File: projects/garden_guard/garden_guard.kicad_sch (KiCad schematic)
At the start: 12 parts, among them J11 USB_C_Receptacle_USB2.0

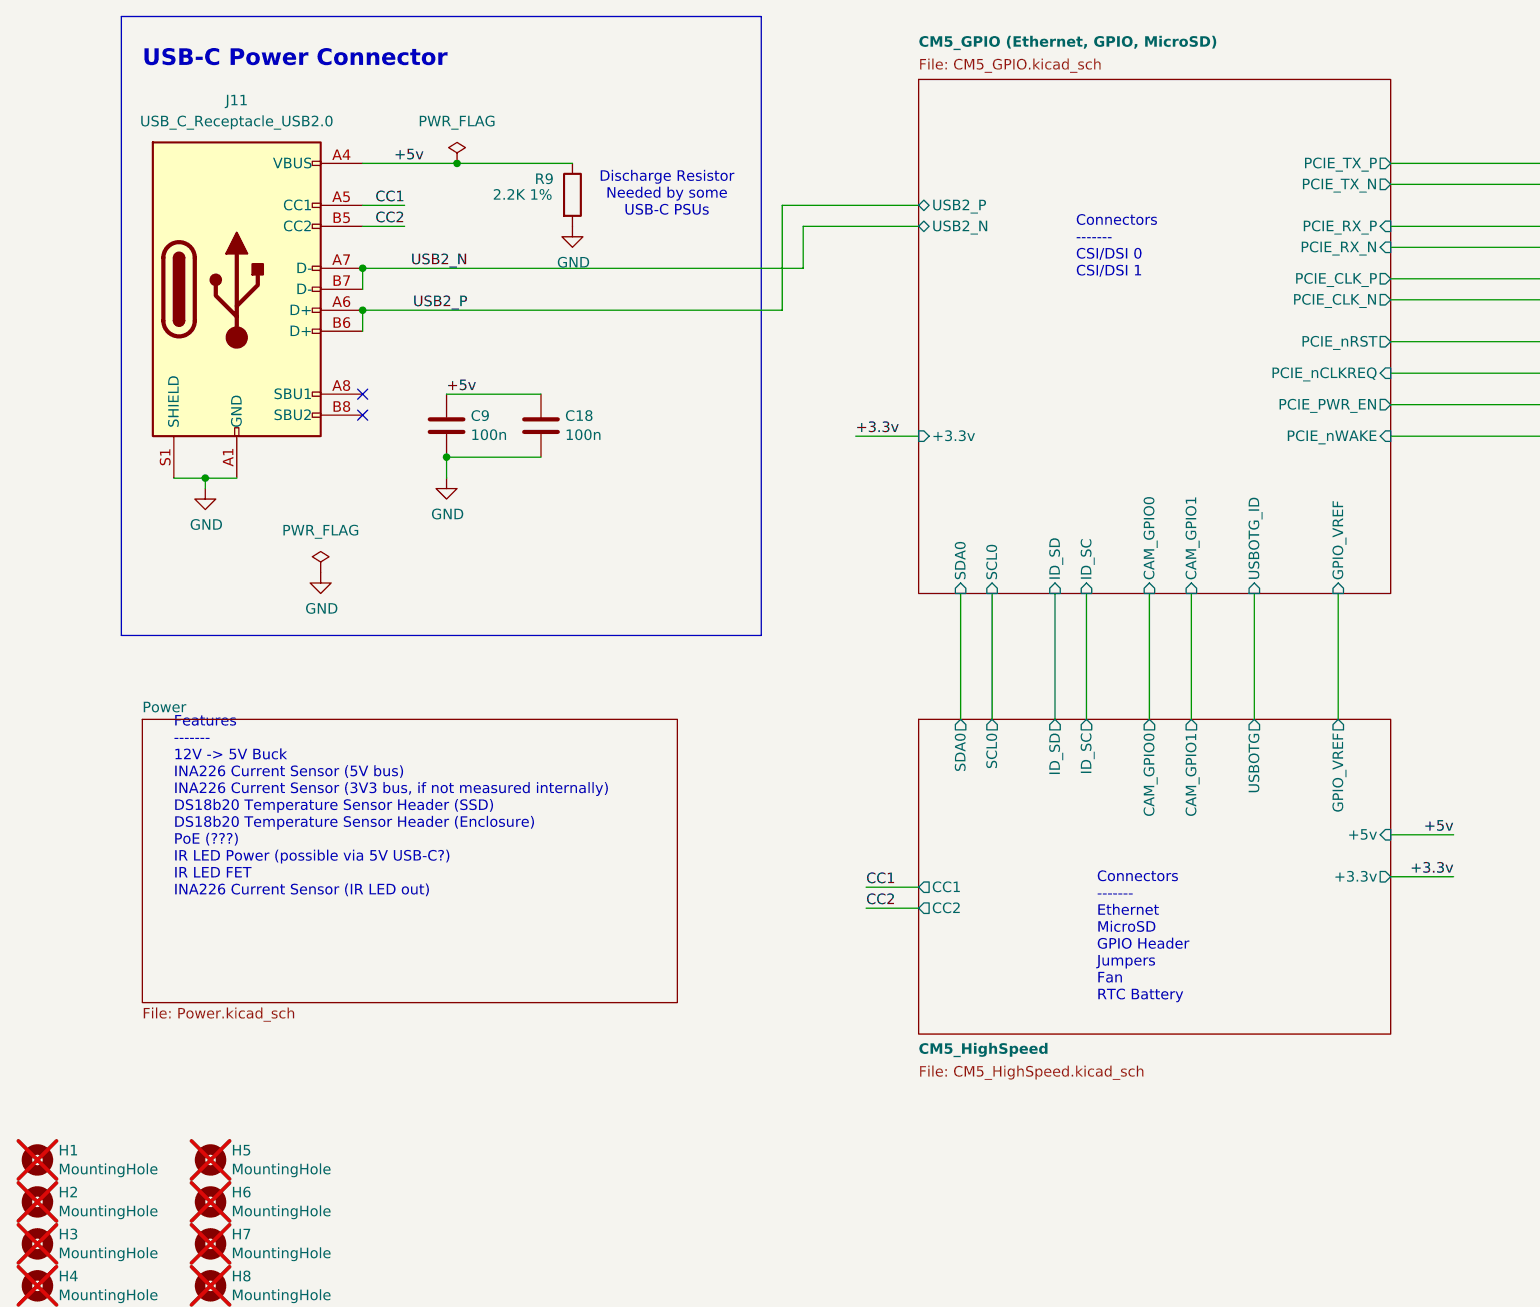
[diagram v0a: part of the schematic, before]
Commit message: - Add PoE 12V power module - Add 12V->5V buck - Add automatic power source selection between PoE 5V and USB 5V
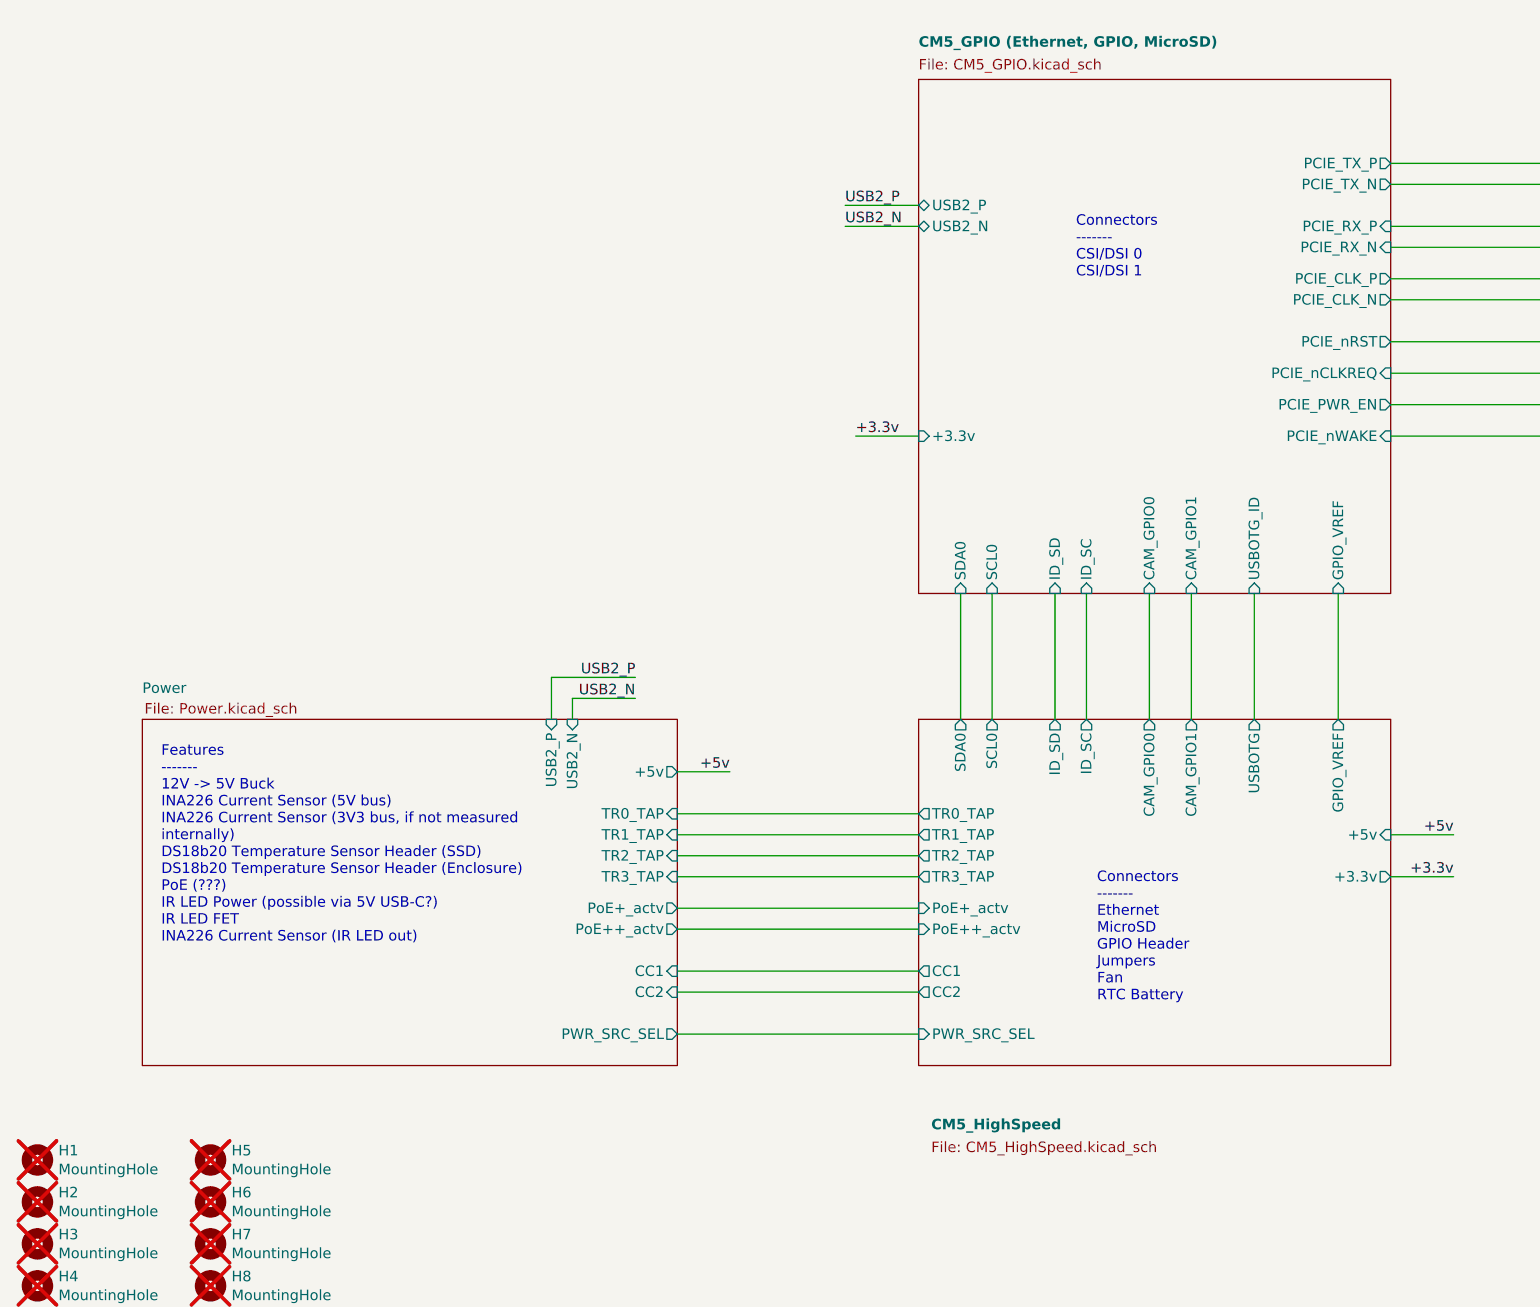
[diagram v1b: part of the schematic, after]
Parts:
- removed C18, C9: 100n, Capacitor_SMD:C_0402_1005Metric, symbol Device:C
- removed J11: USB_C_Receptacle_USB2.0, Connector_USB:USB_C_Receptacle_GCT_USB4105-xx-A_16P_TopMnt_Horizontal, symbol Connector:USB_C_Receptacle_USB2.0_16P
- removed R9: 2.2K 1%, Resistor_SMD:R_0402_1005Metric, symbol Device:R
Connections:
- no-connect marks 2 -> 0
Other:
- sheet CM5_HighSpeed ports: added PWR_SRC_SEL, PoE++_actv, PoE+_actv, TR0_TAP, TR1_TAP, TR2_TAP, TR3_TAP; removed none
- sheet Power ports: added +5v, CC1, CC2, PWR_SRC_SEL, PoE++_actv, PoE+_actv, TR0_TAP, TR1_TAP, TR2_TAP, TR3_TAP, USB2_N, USB2_P; removed none
- note removed: "Discharge Resistor Needed by some USB-C PSUs"
- note removed: "USB-C Power Connector"

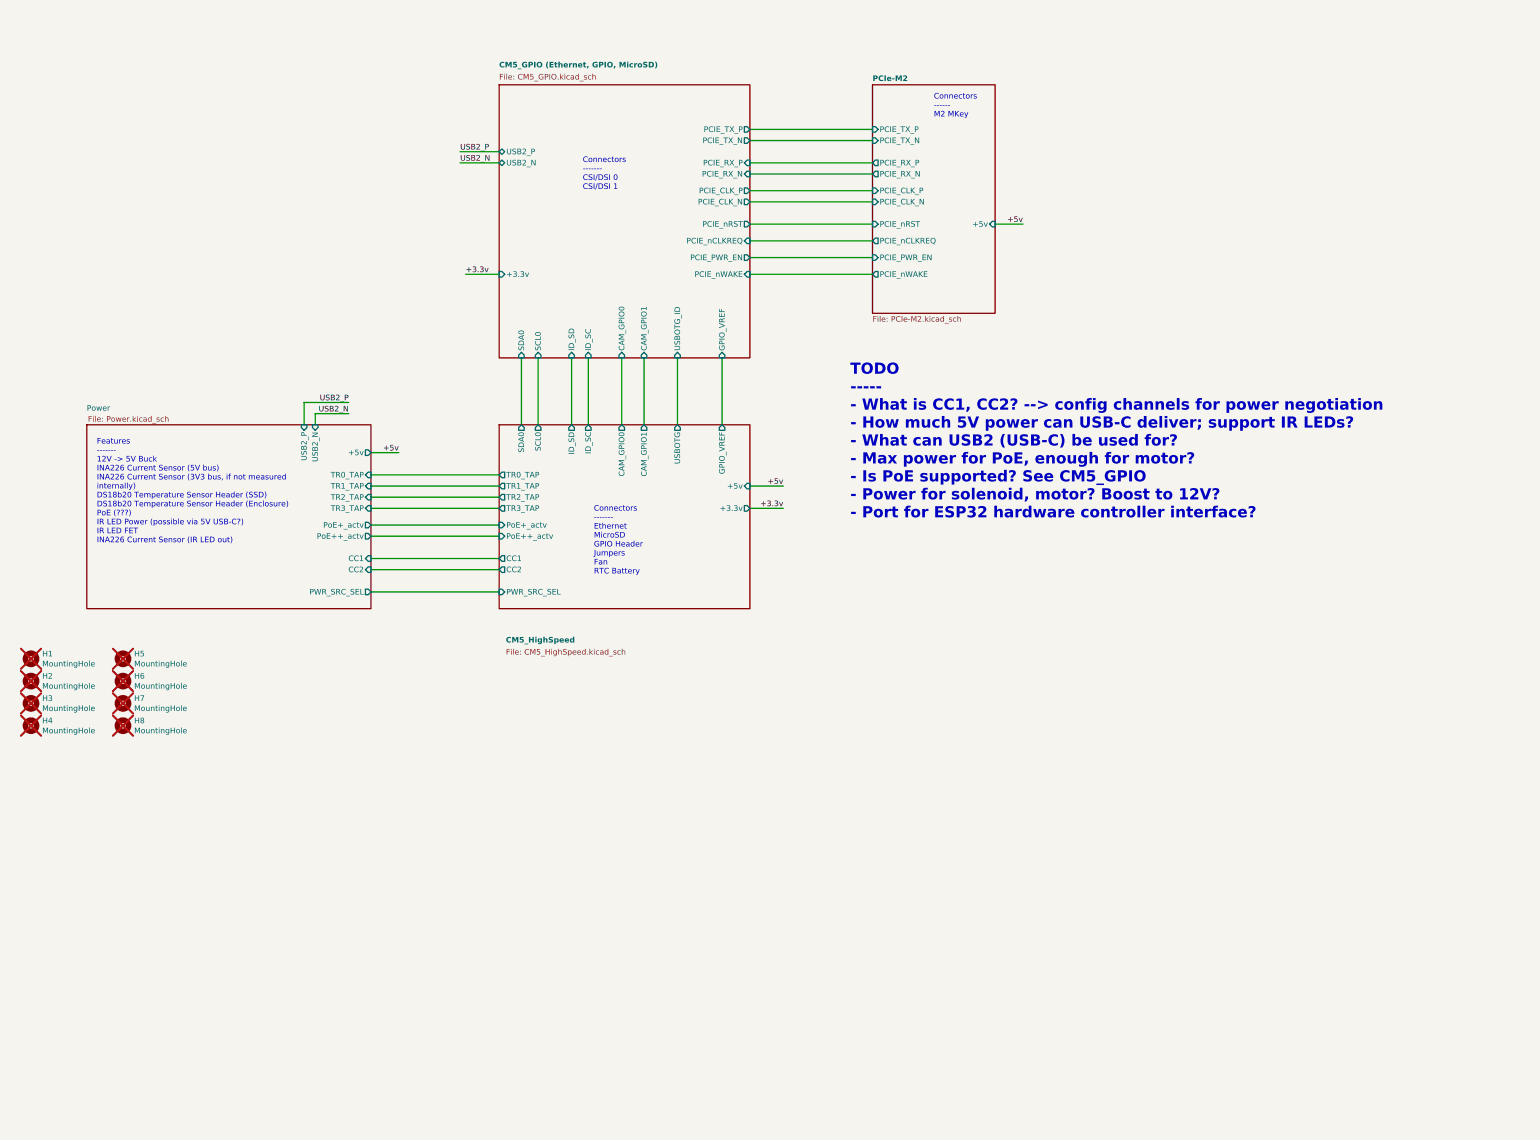
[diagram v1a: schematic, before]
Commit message: - Add 12V and 5V power sensing - Add solenoid and IR illum outputs, power expansion, an peripheral comms - General clean-up - Remove .bak files mistakenly added in previous commits - Add *.bak to .gitignore
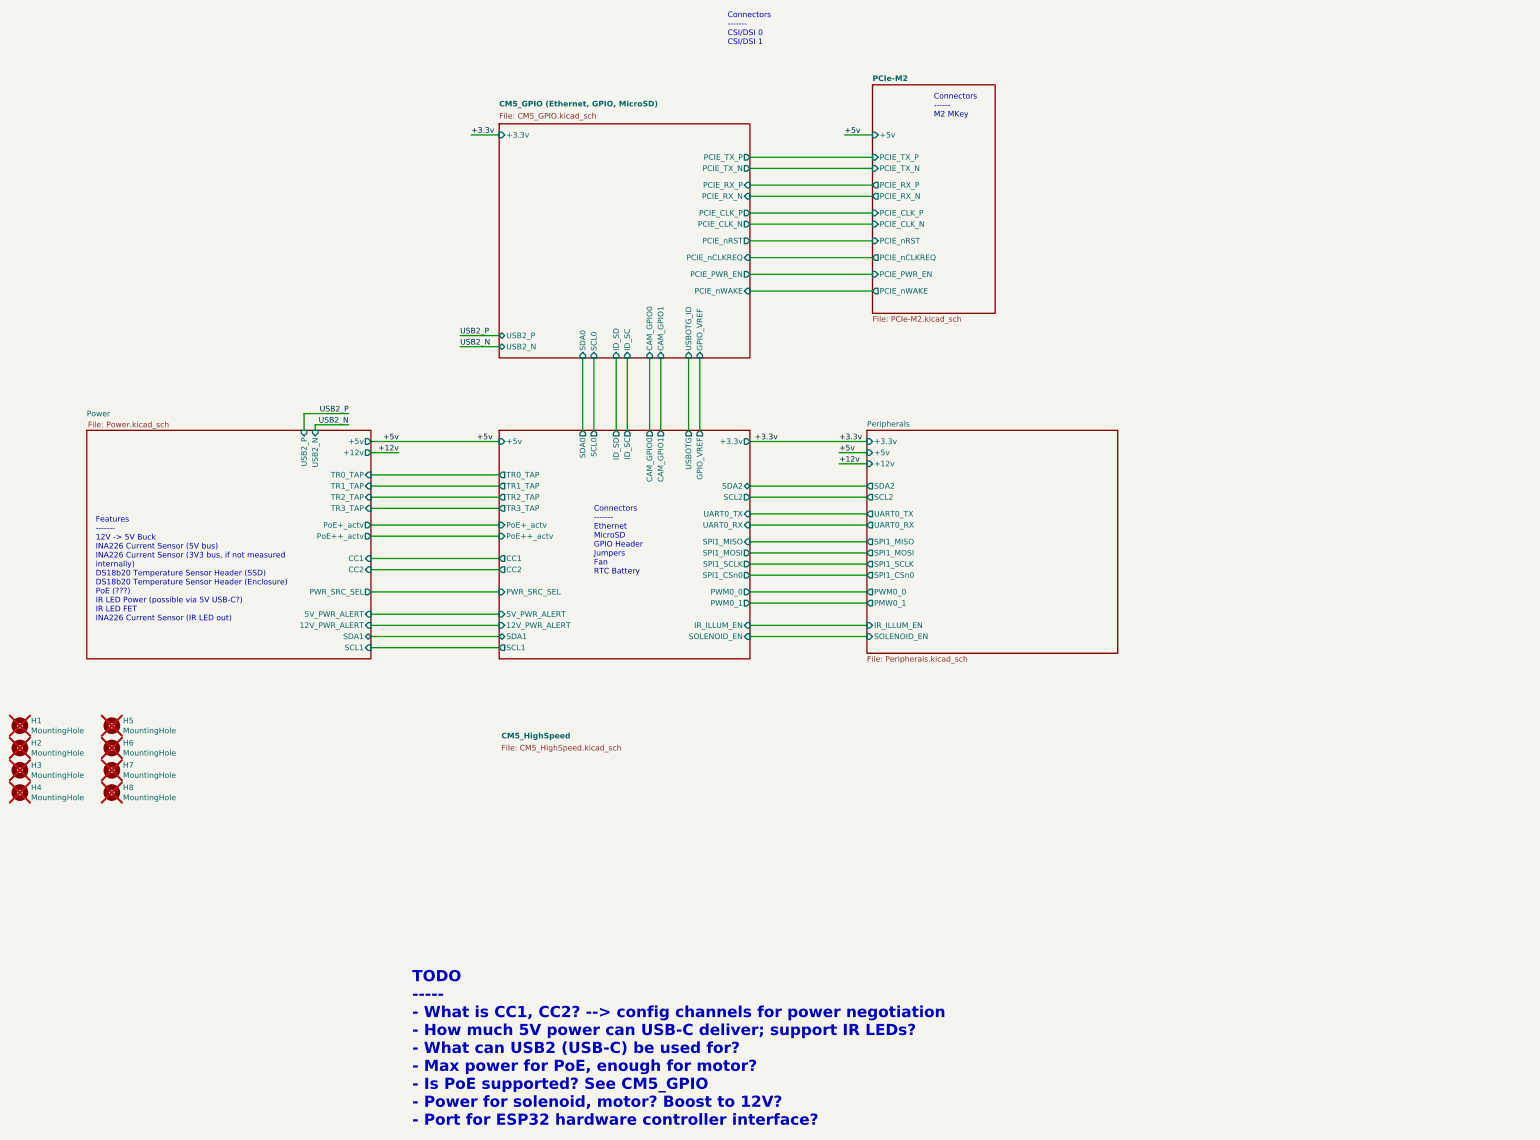
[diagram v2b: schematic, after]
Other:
- added sheet Peripherals (Peripherals.kicad_sch)
- sheet CM5_HighSpeed ports: added 12V_PWR_ALERT, 5V_PWR_ALERT, IR_ILLUM_EN, PWM0_0, PWM0_1, SCL1, SCL2, SDA1, SDA2, SOLENOID_EN, SPI1_CSn0, SPI1_MISO, SPI1_MOSI, SPI1_SCLK, UART0_RX, UART0_TX; removed none
- sheet Power ports: added +12v, 12V_PWR_ALERT, 5V_PWR_ALERT, SCL1, SDA1; removed none
- moved on the sheet: H1, H2, H3, H4, H5, H6, H7, H8

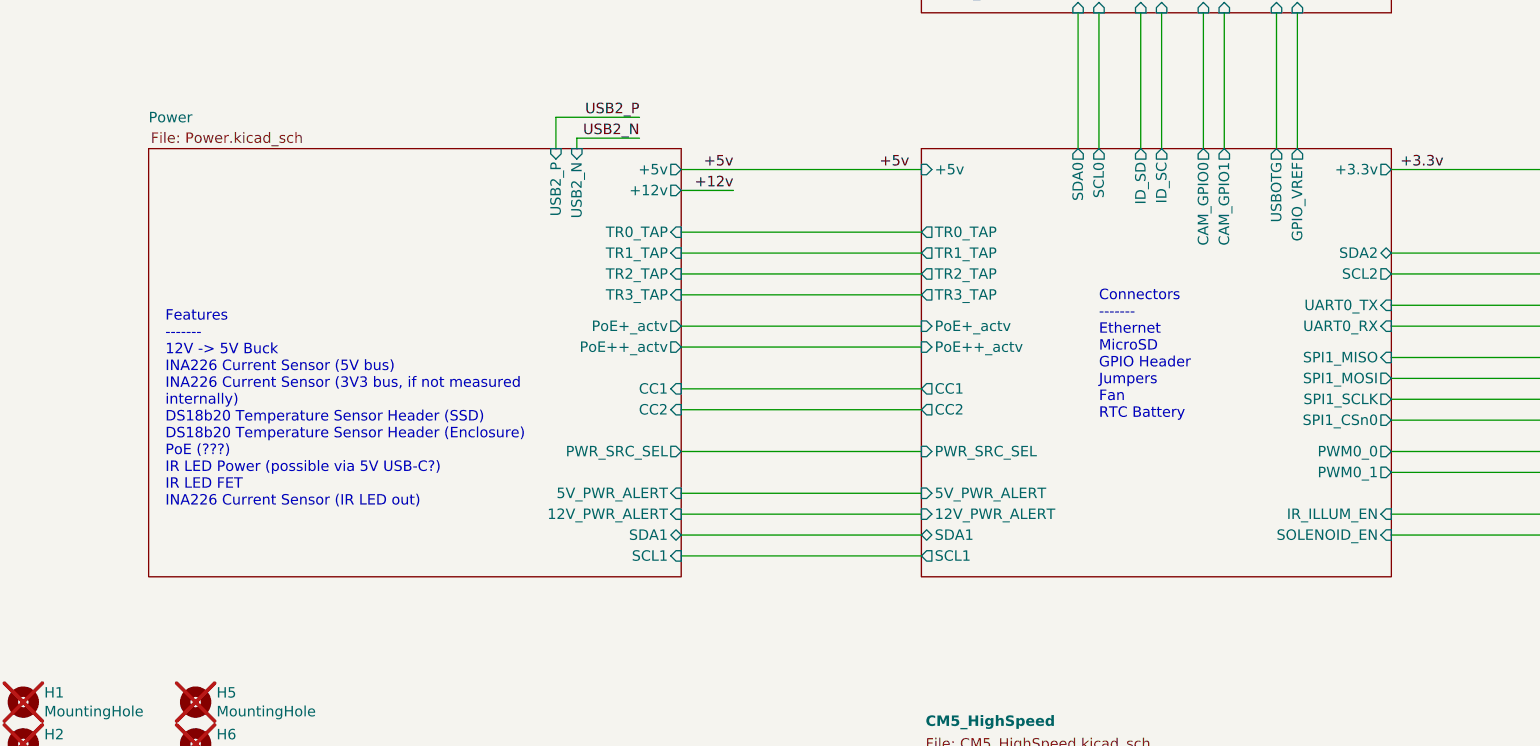
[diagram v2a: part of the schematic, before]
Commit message: - Add all missing footprints - Add specific part numbers to each component in schematic
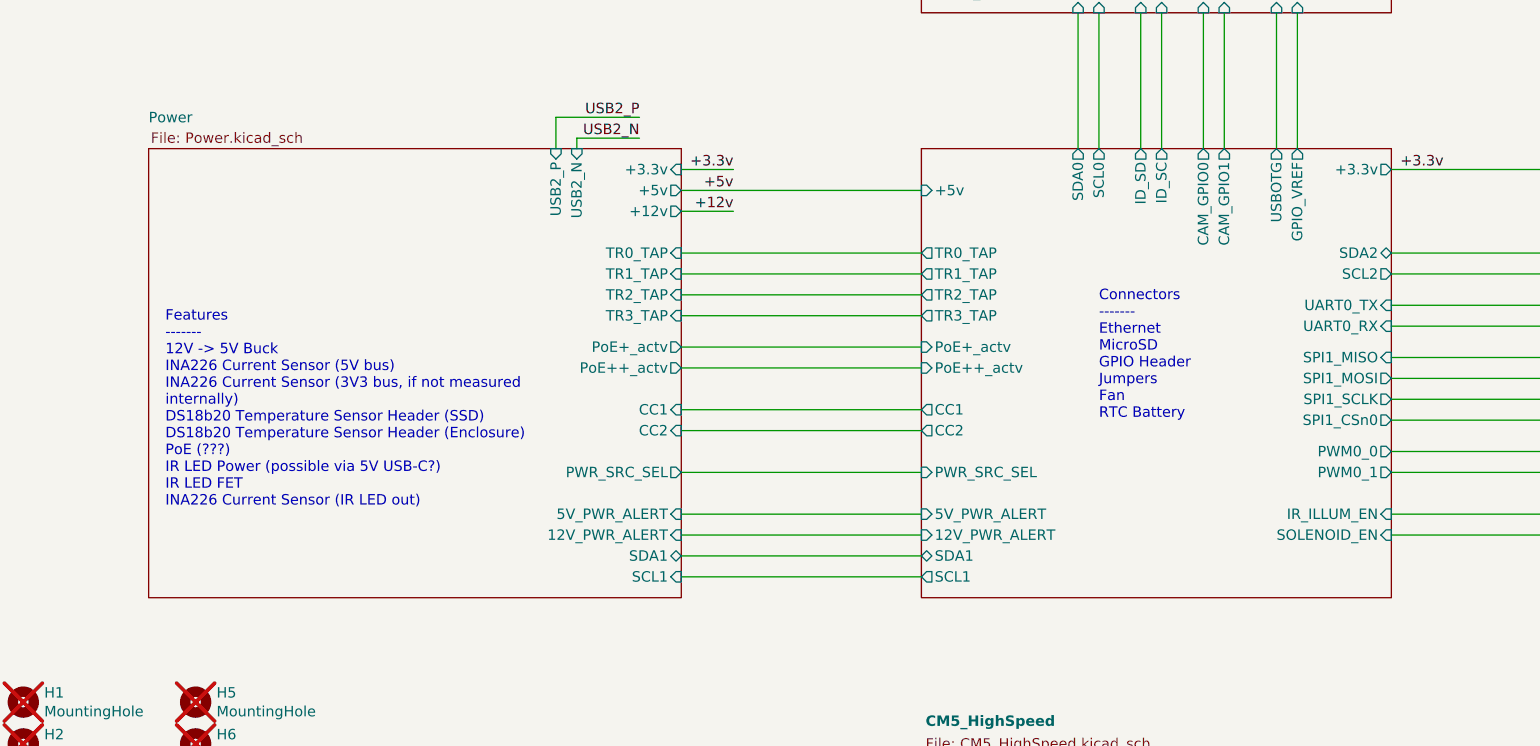
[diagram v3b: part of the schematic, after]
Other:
- sheet Power ports: added +3.3v; removed none
